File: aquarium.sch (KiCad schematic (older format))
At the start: 34 parts

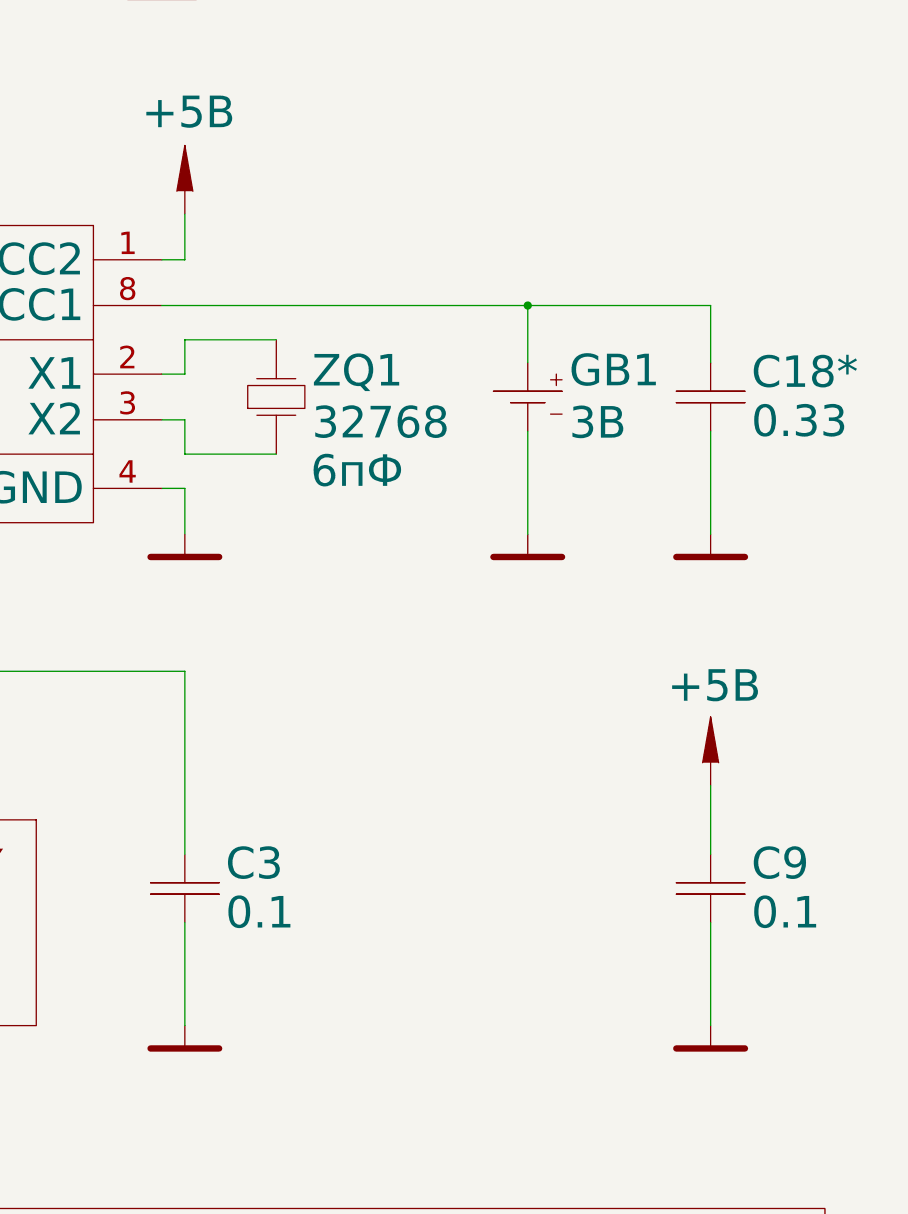
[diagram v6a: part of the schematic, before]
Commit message: Remove optional capacitor from schematic.
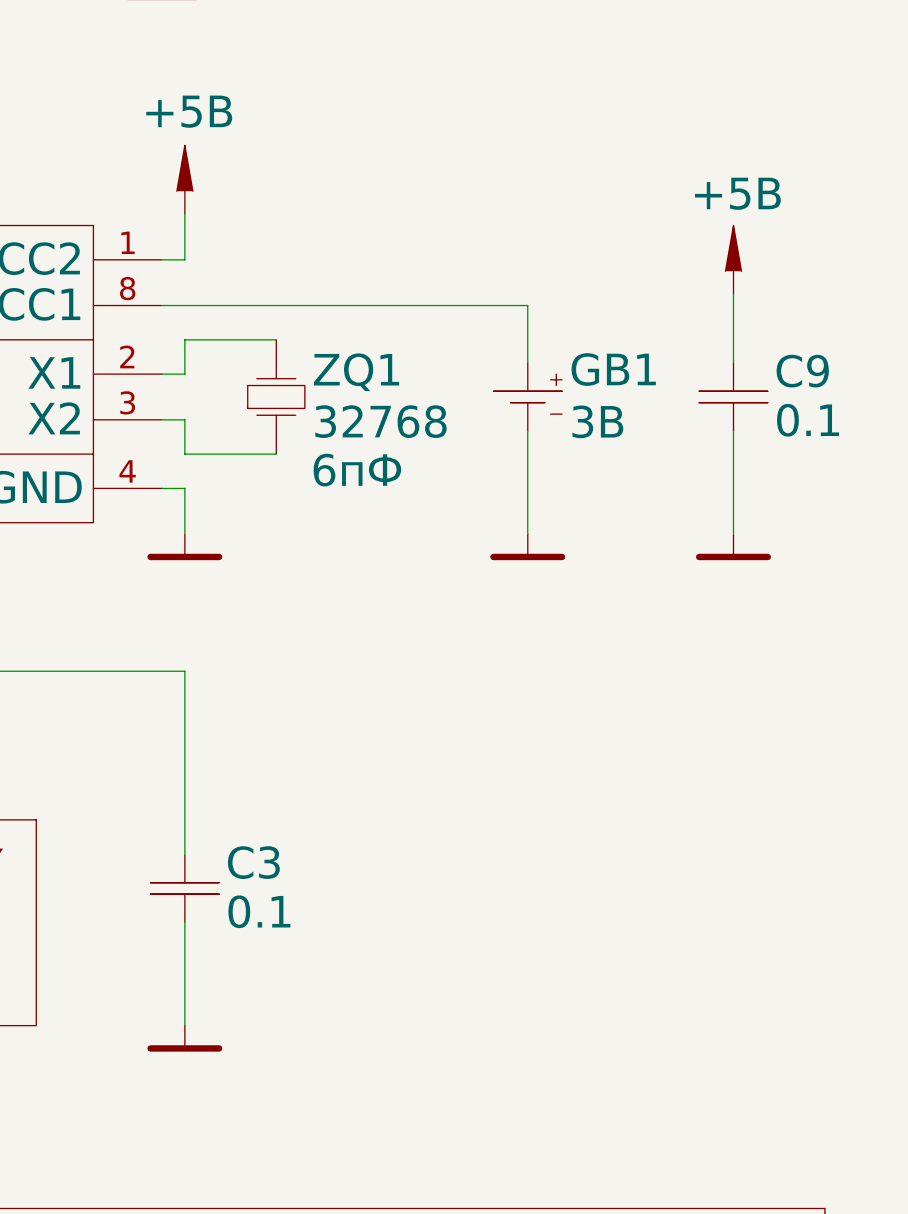
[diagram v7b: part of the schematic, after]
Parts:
- removed C18*: 0.33, Конденсаторы:SMD_0805, symbol C
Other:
- moved on the sheet: C9
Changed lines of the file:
@@
 L C C9
 U 1 1 5679539A
-P 11000 12600
-F 0 "C9" H 11178 12708 138 0000 L CNN
-F 1 "0.1" H 11178 12493 138 0000 L CNN
-F 2 "Конденсаторы:SMD_0805" H 11000 12625 60  0001 C CNN
-F 3 "" H 11000 12625 60  0000 C CNN
-	1    11000 12600
+P 11100 10450
+F 0 "C9" H 11278 10558 138 0000 L CNN
+F 1 "0.1" H 11278 10343 138 0000 L CNN
+F 2 "Конденсаторы:SMD_0805" H 11100 10475 60  0001 C CNN
+F 3 "" H 11100 10475 60  0000 C CNN
+	1    11100 10450
 	1    0    0    -1
 $EndComp
@@
 L GND #PWR24
 U 1 1 567953A0
-P 11000 13200
-F 0 "#PWR24" H 11400 13200 138 0001 C CNN
-F 1 "GND" H 10650 13200 138 0001 C CNN
-F 2 "" H 11000 13200 60  0000 C CNN
-F 3 "" H 11000 13200 60  0000 C CNN
-	1    11000 13200
+P 11100 11050
+F 0 "#PWR24" H 11500 11050 138 0001 C CNN
+F 1 "GND" H 10750 11050 138 0001 C CNN
+F 2 "" H 11100 11050 60  0000 C CNN
+F 3 "" H 11100 11050 60  0000 C CNN
+	1    11100 11050
 	-1   0    0    -1
 $EndComp
@@
 L +5B #PWR23
 U 1 1 567953A6
-P 11000 12150
-F 0 "#PWR23" H 11500 12250 138 0001 C CNN
-F 1 "+5B" H 10984 12585 138 0000 C CNN
-F 2 "" H 11000 12350 60  0000 C CNN
-F 3 "" H 11000 12350 60  0000 C CNN
-	1    11000 12150
-	-1   0    0    -1
-$EndComp
-Wire Wire Line
-	11000 12150 11000 12450
-Wire Wire Line
-	11000 12750 11000 13200
+P 11100 10000
+F 0 "#PWR23" H 11600 10100 138 0001 C CNN
+F 1 "+5B" H 11084 10435 138 0000 C CNN
+F 2 "" H 11100 10200 60  0000 C CNN
+F 3 "" H 11100 10200 60  0000 C CNN
+	1    11100 10000
+	-1   0    0    -1
+$EndComp
+Wire Wire Line
+	11100 10000 11100 10300
+Wire Wire Line
+	11100 10600 11100 11050
 $Comp
 L QUARTZ ZQ1
@@
 Wire Wire Line
 	8700 9850 8600 9850
-Wire Wire Line
-	8600 10050 11000 10050
 $Comp
 L C C5
@@
 	-1   0    0    -1
 $EndComp
-$Comp
-L C C18*
-U 1 1 58C4168F
-P 11000 10450
-F 0 "C18*" H 11178 10558 138 0000 L CNN
-F 1 "0.33" H 11178 10343 138 0000 L CNN
-F 2 "Конденсаторы:SMD_0805" H 11000 10475 60  0001 C CNN
-F 3 "" H 11000 10475 60  0000 C CNN
-	1    11000 10450
-	1    0    0    -1
-$EndComp
-$Comp
-L GND #PWR22
-U 1 1 58C41695
-P 11000 11050
-F 0 "#PWR22" H 11400 11050 138 0001 C CNN
-F 1 "GND" H 10650 11050 138 0001 C CNN
-F 2 "" H 11000 11050 60  0000 C CNN
-F 3 "" H 11000 11050 60  0000 C CNN
-	1    11000 11050
-	-1   0    0    -1
-$EndComp
-Wire Wire Line
-	11000 10050 11000 10300
-Wire Wire Line
-	11000 10600 11000 11050
-Connection ~ 10200 10050
+Wire Wire Line
+	10200 10050 8600 10050
 $EndSCHEMATC

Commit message: README totally reworked.
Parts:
- GB1: value 3В -> 3V
- ZQ1: Тип 6пФ -> 6pF
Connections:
- net +12B renamed +12V
- net +5B renamed +5V
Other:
- note added: "+12V"
- note added: "+5V"
- note added: "HEAT"
- note added: "LIGHT (+)"
- note added: "LIGHT (-)"
- note removed: "+12В"
- note removed: "+5В"
- note removed: "Общ."
- note removed: "Свет (+)"
- note removed: "Свет (-)"
- note removed: "Упр. нагр."
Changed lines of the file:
@@
-EESchema Schematic File Version 2
+EESchema Schematic File Version 3
 LIBS:power
 LIBS:Выключатели_и_кнопки
@@
 $EndComp
 $Comp
-L GND #PWR17
+L GND #PWR017
 U 1 1 56791BEA
 P 9500 1550
-F 0 "#PWR17" H 9900 1550 138 0001 C CNN
+F 0 "#PWR017" H 9900 1550 138 0001 C CNN
 F 1 "GND" H 9150 1550 138 0001 C CNN
 F 2 "" H 9500 1550 60  0000 C CNN
@@
 $EndComp
 $Comp
-L GND #PWR19
+L GND #PWR019
 U 1 1 56791C0B
 P 10200 1550
-F 0 "#PWR19" H 10600 1550 138 0001 C CNN
+F 0 "#PWR019" H 10600 1550 138 0001 C CNN
 F 1 "GND" H 9850 1550 138 0001 C CNN
 F 2 "" H 10200 1550 60  0000 C CNN
@@
 $EndComp
 $Comp
-L +5B #PWR16
+L +5V #PWR016
 U 1 1 56791C40
 P 9500 750
-F 0 "#PWR16" H 10000 850 138 0001 C CNN
-F 1 "+5B" H 9484 1185 138 0000 C CNN
+F 0 "#PWR016" H 10000 850 138 0001 C CNN
+F 1 "+5V" H 9484 1185 138 0000 C CNN
 F 2 "" H 9500 950 60  0000 C CNN
 F 3 "" H 9500 950 60  0000 C CNN
@@
 $EndComp
 $Comp
-L +5B #PWR18
+L +5V #PWR018
 U 1 1 56791C61
 P 10200 750
-F 0 "#PWR18" H 10700 850 138 0001 C CNN
-F 1 "+5B" H 10184 1185 138 0000 C CNN
+F 0 "#PWR018" H 10700 850 138 0001 C CNN
+F 1 "+5V" H 10184 1185 138 0000 C CNN
 F 2 "" H 10200 950 60  0000 C CNN
 F 3 "" H 10200 950 60  0000 C CNN
@@
 	10200 1300 10200 1550
 $Comp
-L +5B #PWR14
+L +5V #PWR014
 U 1 1 56791F4C
 P 8750 750
-F 0 "#PWR14" H 9250 850 138 0001 C CNN
-F 1 "+5B" H 8734 1185 138 0000 C CNN
+F 0 "#PWR014" H 9250 850 138 0001 C CNN
+F 1 "+5V" H 8734 1185 138 0000 C CNN
 F 2 "" H 8750 950 60  0000 C CNN
 F 3 "" H 8750 950 60  0000 C CNN
@@
 Connection ~ 8750 950
 $Comp
-L GND #PWR15
+L GND #PWR015
 U 1 1 567920EA
 P 8750 4550
-F 0 "#PWR15" H 9150 4550 138 0001 C CNN
+F 0 "#PWR015" H 9150 4550 138 0001 C CNN
 F 1 "GND" H 8400 4550 138 0001 C CNN
 F 2 "" H 8750 4550 60  0000 C CNN
@@
 $EndComp
 $Comp
-L GND #PWR6
+L GND #PWR06
 U 1 1 56795326
 P 5350 6250
-F 0 "#PWR6" H 5750 6250 138 0001 C CNN
+F 0 "#PWR06" H 5750 6250 138 0001 C CNN
 F 1 "GND" H 5000 6250 138 0001 C CNN
 F 2 "" H 5350 6250 60  0000 C CNN
@@
 $EndComp
 $Comp
-L GND #PWR24
+L GND #PWR024
 U 1 1 567953A0
 P 11100 11050
-F 0 "#PWR24" H 11500 11050 138 0001 C CNN
+F 0 "#PWR024" H 11500 11050 138 0001 C CNN
 F 1 "GND" H 10750 11050 138 0001 C CNN
 F 2 "" H 11100 11050 60  0000 C CNN
@@
 $EndComp
 $Comp
-L +5B #PWR23
+L +5V #PWR023
 U 1 1 567953A6
 P 11100 10000
-F 0 "#PWR23" H 11600 10100 138 0001 C CNN
-F 1 "+5B" H 11084 10435 138 0000 C CNN
+F 0 "#PWR023" H 11600 10100 138 0001 C CNN
+F 1 "+5V" H 11084 10435 138 0000 C CNN
 F 2 "" H 11100 10200 60  0000 C CNN
 F 3 "" H 11100 10200 60  0000 C CNN
@@
 F 2 "Прочее:HC_3.0x8.0mm" H 9100 10450 60  0001 C CNN
 F 3 "" H 9100 10450 60  0000 C CNN
-F 4 "6пФ" V 8775 10300 138 0000 R CNN "Тип"
+F 4 "6pF" V 8775 10300 138 0000 R CNN "Тип"
 	1    9100 10450
 	0    -1   -1   0
@@
 	8700 10200 9100 10200
 $Comp
-L +5B #PWR11
+L +5V #PWR011
 U 1 1 56797DB1
 P 8700 9650
-F 0 "#PWR11" H 9200 9750 138 0001 C CNN
-F 1 "+5B" H 8684 10094 138 0000 C CNN
+F 0 "#PWR011" H 9200 9750 138 0001 C CNN
+F 1 "+5V" H 8684 10094 138 0000 C CNN
 F 2 "" H 8700 9850 60  0000 C CNN
 F 3 "" H 8700 9850 60  0000 C CNN
@@
 $EndComp
 $Comp
-L GND #PWR12
+L GND #PWR012
 U 1 1 5679847B
 P 8700 11050
-F 0 "#PWR12" H 9100 11050 138 0001 C CNN
+F 0 "#PWR012" H 9100 11050 138 0001 C CNN
 F 1 "GND" H 8350 11050 138 0001 C CNN
 F 2 "" H 8700 11050 60  0000 C CNN
@@
 	9600 6350 9600 6250
 $Comp
-L GND #PWR9
+L GND #PWR09
 U 1 1 56798CBF
 P 8600 6650
-F 0 "#PWR9" H 9000 6650 138 0001 C CNN
+F 0 "#PWR09" H 9000 6650 138 0001 C CNN
 F 1 "GND" H 8250 6650 138 0001 C CNN
 F 2 "" H 8600 6650 60  0000 C CNN
@@
 $EndComp
 $Comp
-L GND #PWR8
+L GND #PWR08
 U 1 1 567A531F
 P 6400 13200
-F 0 "#PWR8" H 6800 13200 138 0001 C CNN
+F 0 "#PWR08" H 6800 13200 138 0001 C CNN
 F 1 "GND" H 6050 13200 138 0001 C CNN
 F 2 "" H 6400 13200 60  0000 C CNN
@@
 $EndComp
 Text Notes 400  7275 0    98   ~ 0
-Свет (+)
+LIGHT (+)
 Text Notes 400  7475 0    98   ~ 0
-Свет (-)
+LIGHT (-)
 Text Notes 500  1025 0    98   ~ 0
-+5В
++5V
 Text Notes 575  1625 0    98   ~ 0
 TX
@@
 GND
 $Comp
-L GND #PWR2
+L GND #PWR02
 U 1 1 567D101C
 P 2000 6100
-F 0 "#PWR2" H 2400 6100 138 0001 C CNN
+F 0 "#PWR02" H 2400 6100 138 0001 C CNN
 F 1 "GND" H 1650 6100 138 0001 C CNN
 F 2 "" H 2000 6100 60  0000 C CNN
@@
 	4100 10900 1750 10900
 Text Label 4100 950  2    100  ~ 0
-+5B
++5V
 Text Label 4100 1550 2    100  ~ 0
 TX
@@
 MISO
 Text Label 4100 3050 2    100  ~ 0
-+5B
++5V
 Text Label 4100 3650 2    100  ~ 0
 SCK
@@
 S 200  14000 11300 2300
 U 58476793
-F0 "Блок питания" 138
+F0 "Power supply" 138
 F1 "power.sch" 100
 $EndSheet
 $Comp
-L GND #PWR20
+L GND #PWR020
 U 1 1 58491DD9
 P 10200 11050
-F 0 "#PWR20" H 10600 11050 138 0001 C CNN
+F 0 "#PWR020" H 10600 11050 138 0001 C CNN
 F 1 "GND" H 9850 11050 138 0001 C CNN
 F 2 "" H 10200 11050 60  0000 C CNN
@@
 $EndComp
 Text Notes 525  5475 0    98   ~ 0
-+5В
-Text Notes 300  5850 0    98   ~ 0
-Упр. нагр.
++5V
+Text Notes 500  5875 0    98   ~ 0
+HEAT
 Text Notes 475  5275 0    98   ~ 0
-+12В
++12V
 Text Notes 525  5675 0    98   ~ 0
-Общ.
+GND
 Text Notes 350  6150 0    138  ~ 0
 POWER
@@
 	2000 11800 2000 11950
 $Comp
-L +5B #PWR4
+L +5V #PWR04
 U 1 1 584B914C
 P 2650 4900
-F 0 "#PWR4" H 3150 5000 138 0001 C CNN
-F 1 "+5B" H 2634 5335 138 0000 C CNN
+F 0 "#PWR04" H 3150 5000 138 0001 C CNN
+F 1 "+5V" H 2634 5335 138 0000 C CNN
 F 2 "" H 2650 5100 60  0000 C CNN
 F 3 "" H 2650 5100 60  0000 C CNN
@@
 	2650 4900 2650 5400
 Wire Wire Line
-	2650 5400 1800 5400
+	1800 5400 4100 5400
 Entry Wire Line
 	4200 11750 4300 11650
@@
 $EndComp
 $Comp
-L GND #PWR13
+L GND #PWR013
 U 1 1 584EFF17
 P 8700 13200
-F 0 "#PWR13" H 9100 13200 138 0001 C CNN
+F 0 "#PWR013" H 9100 13200 138 0001 C CNN
 F 1 "GND" H 8350 13200 138 0001 C CNN
 F 2 "" H 8700 13200 60  0000 C CNN
@@
 Connection ~ 6400 11650
 $Comp
-L +12B #PWR1
+L +12V #PWR01
 U 1 1 58470EC2
 P 2000 4900
-F 0 "#PWR1" H 2500 5000 138 0001 C CNN
-F 1 "+12B" H 1987 5345 138 0000 C CNN
+F 0 "#PWR01" H 2500 5000 138 0001 C CNN
+F 1 "+12V" H 1987 5345 138 0000 C CNN
 F 2 "" H 2000 5100 60  0000 C CNN
 F 3 "" H 2000 5100 60  0000 C CNN
@@
 	2000 4900 2000 5200
 $Comp
-L +12B #PWR5
+L +12V #PWR05
 U 1 1 586A2E7C
 P 2650 6900
-F 0 "#PWR5" H 3150 7000 138 0001 C CNN
-F 1 "+12B" H 2637 7345 138 0000 C CNN
+F 0 "#PWR05" H 3150 7000 138 0001 C CNN
+F 1 "+12V" H 2637 7345 138 0000 C CNN
 F 2 "" H 2650 7100 60  0000 C CNN
 F 3 "" H 2650 7100 60  0000 C CNN
@@
 	2000 7400 2000 7700
 $Comp
-L GND #PWR3
+L GND #PWR03
 U 1 1 586A3FC9
 P 2000 8700
-F 0 "#PWR3" H 2400 8700 138 0001 C CNN
+F 0 "#PWR03" H 2400 8700 138 0001 C CNN
 F 1 "GND" H 1650 8700 138 0001 C CNN
 F 2 "" H 2000 8700 60  0000 C CNN
@@
 $EndComp
 $Comp
-L GND #PWR7
+L GND #PWR07
 U 1 1 586F73E8
 P 5350 8200
-F 0 "#PWR7" H 5750 8200 138 0001 C CNN
+F 0 "#PWR07" H 5750 8200 138 0001 C CNN
 F 1 "GND" H 5000 8200 138 0001 C CNN
 F 2 "" H 5350 8200 60  0000 C CNN
@@
 	9600 8300 9600 8200
 $Comp
-L GND #PWR10
+L GND #PWR010
 U 1 1 586F7403
 P 8600 8600
-F 0 "#PWR10" H 9000 8600 138 0001 C CNN
+F 0 "#PWR010" H 9000 8600 138 0001 C CNN
 F 1 "GND" H 8250 8600 138 0001 C CNN
 F 2 "" H 8600 8600 60  0000 C CNN
@@
 $EndComp
 $Comp
-L GND #PWR21
+L GND #PWR021
 U 1 1 586F79F4
 P 10800 1550
-F 0 "#PWR21" H 11200 1550 138 0001 C CNN
+F 0 "#PWR021" H 11200 1550 138 0001 C CNN
 F 1 "GND" H 10450 1550 138 0001 C CNN
 F 2 "" H 10800 1550 60  0000 C CNN
@@
 P 10200 10450
 F 0 "GB1" H 10381 10565 138 0000 L CNN
-F 1 "3В" H 10381 10336 138 0000 L CNN
+F 1 "3V" H 10381 10336 138 0000 L CNN
 F 2 "Разъемы:CR2032_H" H 10200 10475 60  0001 C CNN
 F 3 "" H 10200 10475 60  0000 C CNN
@@
 Wire Wire Line
 	10200 10050 8600 10050
+Entry Wire Line
+	4100 5400 4200 5500
+Connection ~ 2650 5400
+Text Label 4100 5400 2    100  ~ 0
++5V
 $EndSCHEMATC
